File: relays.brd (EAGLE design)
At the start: 111.8 x 48.3 mm, 45 parts, among them Q1 MMBT2222A, Q2 MMBT2222A, T1 BTA12-600, T2 BTA12-600

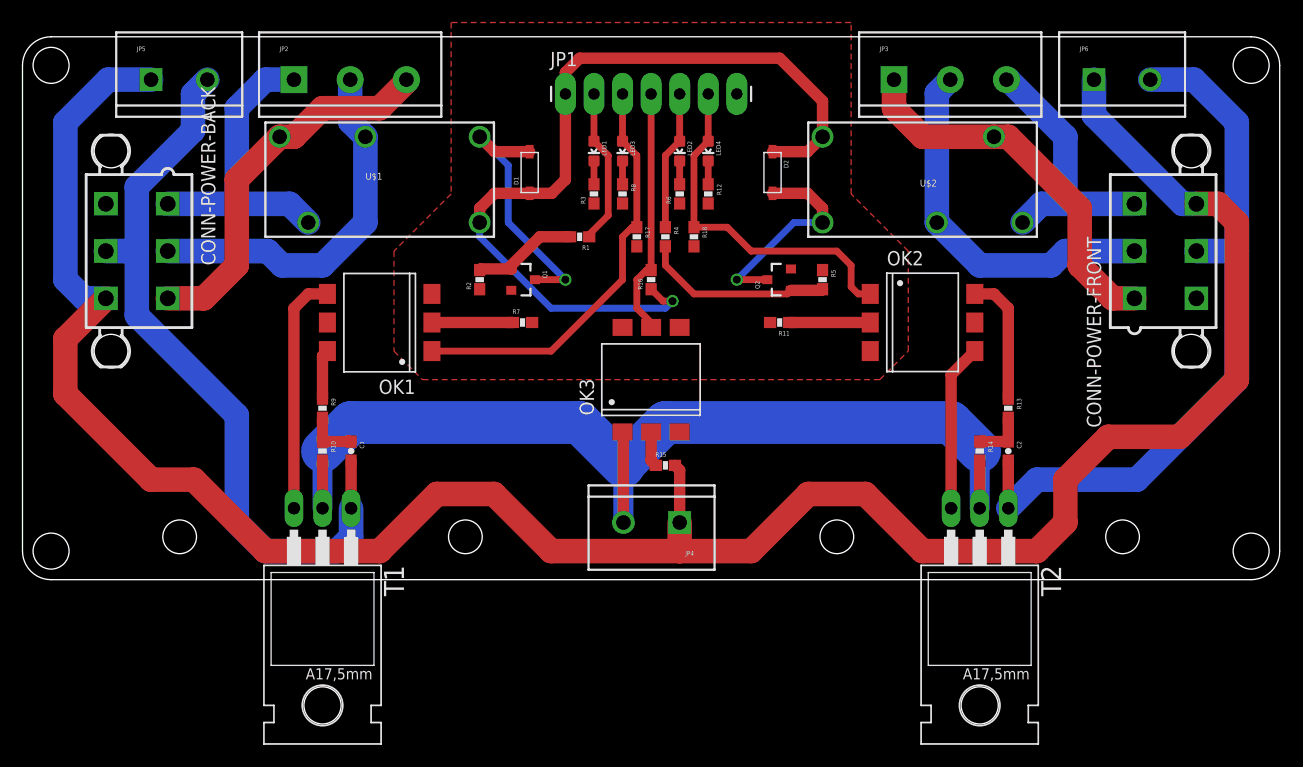
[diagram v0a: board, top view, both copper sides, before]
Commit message: add some silkscreen
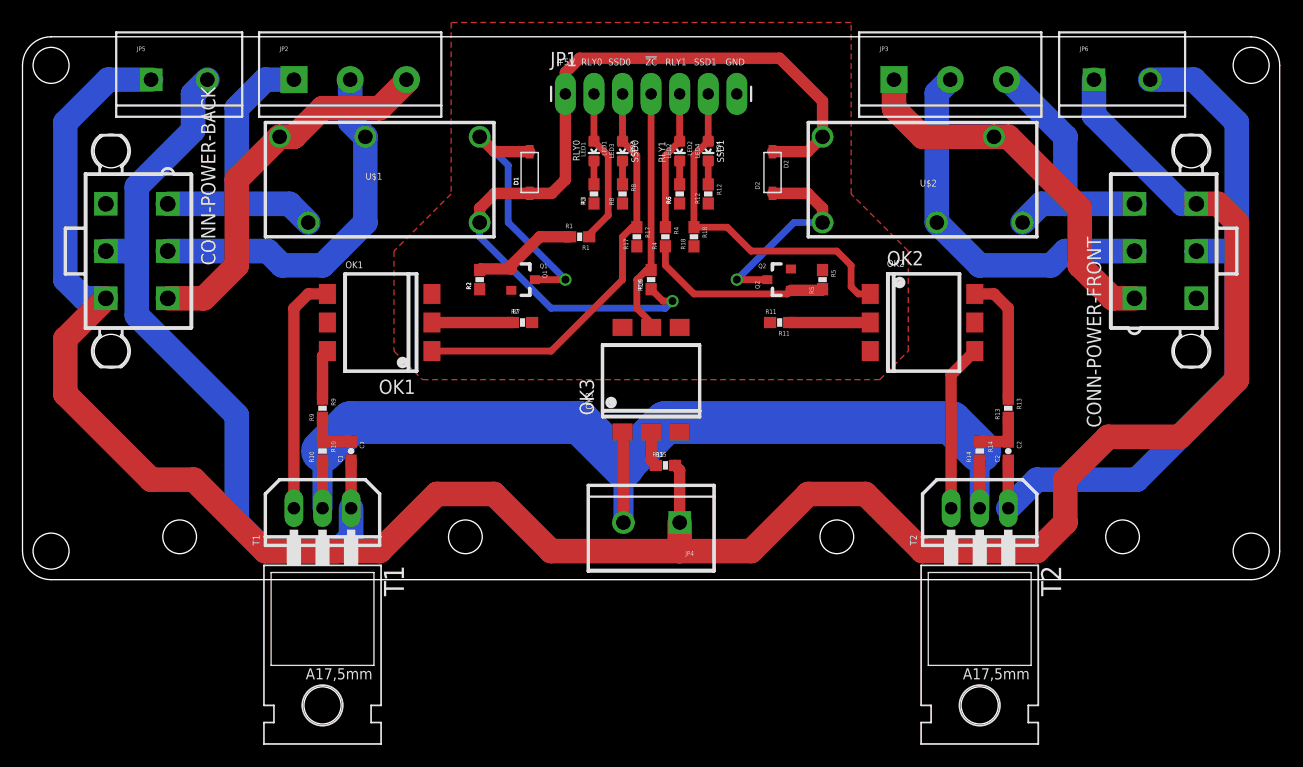
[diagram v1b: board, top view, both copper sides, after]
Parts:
- OK3: value MOC3020 -> H11AA1
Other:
- board text added: "!ZC"
- board text added: "+5V"
- board text added: "C1"
- board text added: "C2"
- board text added: "D1"
- board text added: "D2"
- board text added: "GND"
- board text added: "LED1"
- board text added: "LED2"
- board text added: "LED3"
- board text added: "LED4"
- board text added: "OK1"
- board text added: "OK2"
- board text added: "OK3"
- board text added: "Q1"
- board text added: "Q2"
- board text added: "R1"
- board text added: "R10"
- board text added: "R11"
- board text added: "R12"
- board text added: "R13"
- board text added: "R14"
- board text added: "R15"
- board text added: "R16"
- board text added: "R17"
- board text added: "R18"
- board text added: "R2"
- board text added: "R3"
- board text added: "R4"
- board text added: "R5"
- board text added: "R6"
- board text added: "R7"
- board text added: "R8"
- board text added: "R9"
- board text added: "RLY0"
- board text added: "RLY1"
- board text added: "SSD0"
- board text added: "SSD1"
- board text added: "T1"
- board text added: "T2"

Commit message: update relay board, REx. Good boy.
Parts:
- renumbered U$1 to RELAY0, U$2 to RELAY1
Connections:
- net SSD0-HOT renamed SSR0-HOT
- net SSD1-HOT renamed SSR1-HOT
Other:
- board text added: "AC NEUT"
- board text added: "AC-HOT"
- board text added: "AC-NEUT"
- board text added: "DANGER!"
- board text added: "HIGH VOLTAGE!"
- board text added: "Iridium REx"
- board text added: "NC"
- board text added: "NO"
- board text added: "RELAY0"
- board text added: "RELAY1"
- board text added: "RL0"
- board text added: "RL0 LOAD"
- board text added: "RL0 NC"
- board text added: "RL0 NO"
- board text added: "RL1"
- board text added: "RL1 LOAD"
- board text added: "RL1 NC"
- board text added: "RL1 NO"
- board text added: "SS0"
- board text added: "SS1"
- board text added: "SSR0 HOT"
- board text added: "SSR0-HOT"
- board text added: "SSR1 HOT"
- board text added: "SSR1-HOT"
- board text added: "rev 0.1"
- board text removed: "RLY0"
- board text removed: "RLY1"
- board text removed: "SSD0"
- board text removed: "SSD1"
